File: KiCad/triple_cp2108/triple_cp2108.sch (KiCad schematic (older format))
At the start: 18 parts

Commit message: Parts importing in prgs.
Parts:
- gave numbers to parts that had none: 18
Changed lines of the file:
@@
 $EndDescr
 $Comp
-L Connector:USB_B J?
+L Connector:USB_B J1
 U 1 1 5FE5590A
 P 750 1000
-F 0 "J?" H 807 1467 50  0000 C CNN
+F 0 "J1" H 807 1467 50  0000 C CNN
 F 1 "USB_B" H 807 1376 50  0000 C CNN
 F 2 "" H 900 950 50  0001 C CNN
@@
 NoConn ~ 650  1400
 $Comp
-L power:GND #PWR?
+L power:GND #PWR0101
 U 1 1 5FE56D8C
 P 750 1700
-F 0 "#PWR?" H 750 1450 50  0001 C CNN
+F 0 "#PWR0101" H 750 1450 50  0001 C CNN
 F 1 "GND" H 755 1527 50  0000 C CNN
 F 2 "" H 750 1700 50  0001 C CNN
@@
 	1500 1100 1900 1100
 $Comp
-L Interface_USB:USB2514B_Bi U?
+L Interface_USB:USB2514B_Bi U2
 U 1 1 5FE587F7
 P 2700 5150
-F 0 "U?" H 3650 3700 50  0000 C CNN
+F 0 "U2" H 3650 3700 50  0000 C CNN
 F 1 "USB2514B_Bi" H 3450 3600 50  0000 C CNN
 F 2 "Package_DFN_QFN:QFN-36-1EP_6x6mm_P0.5mm_EP3.7x3.7mm" H 4000 3650 50  0001 C CNN
@@
 NoConn ~ 3800 6050
 $Comp
-L Regulator_Linear:MIC5504-3.3YM5 U?
+L Regulator_Linear:MIC5504-3.3YM5 U1
 U 1 1 5FE5BDFF
 P 1700 2400
-F 0 "U?" H 1700 2767 50  0000 C CNN
+F 0 "U1" H 1700 2767 50  0000 C CNN
 F 1 "MIC5504-3.3YM5" H 1700 2676 50  0000 C CNN
 F 2 "Package_TO_SOT_SMD:SOT-23-5" H 1700 2000 50  0001 C CNN
@@
 	1700 2700 1700 2800
 $Comp
-L power:GND #PWR?
+L power:GND #PWR0102
 U 1 1 5FE5FD67
 P 1700 2850
-F 0 "#PWR?" H 1700 2600 50  0001 C CNN
+F 0 "#PWR0102" H 1700 2600 50  0001 C CNN
 F 1 "GND" H 1705 2677 50  0000 C CNN
 F 2 "" H 1700 2850 50  0001 C CNN
@@
 $EndComp
 $Comp
-L Device:C C?
+L Device:C C3
 U 1 1 5FE61456
 P 1100 2550
-F 0 "C?" V 1150 2700 50  0000 C CNN
+F 0 "C3" V 1150 2700 50  0000 C CNN
 F 1 "1u" V 1150 2400 50  0000 C CNN
 F 2 "" H 1138 2400 50  0001 C CNN
@@
 	2150 2300 2250 2300
 $Comp
-L Device:C C?
+L Device:C C4
 U 1 1 5FE6AB30
 P 2150 2550
-F 0 "C?" V 2200 2700 50  0000 C CNN
+F 0 "C4" V 2200 2700 50  0000 C CNN
 F 1 "1u" V 2200 2400 50  0000 C CNN
 F 2 "" H 2188 2400 50  0001 C CNN
@@
 	2150 2300 2150 2400
 $Comp
-L Device:C C?
+L Device:C C5
 U 1 1 5FE79D1D
 P 2700 1200
-F 0 "C?" V 2750 1350 50  0000 C CNN
+F 0 "C5" V 2750 1350 50  0000 C CNN
 F 1 "4u7" V 2750 1050 50  0000 C CNN
 F 2 "" H 2738 1050 50  0001 C CNN
@@
 VBUS_5V
 $Comp
-L power:GND #PWR?
+L power:GND #PWR0103
 U 1 1 5FE7AB84
 P 2700 1450
-F 0 "#PWR?" H 2700 1200 50  0001 C CNN
+F 0 "#PWR0103" H 2700 1200 50  0001 C CNN
 F 1 "GND" H 2705 1277 50  0000 C CNN
 F 2 "" H 2700 1450 50  0001 C CNN
@@
 $EndComp
 $Comp
-L Device:C C?
+L Device:C C6
 U 1 1 5FE7B840
 P 2950 1200
-F 0 "C?" V 3000 1350 50  0000 C CNN
+F 0 "C6" V 3000 1350 50  0000 C CNN
 F 1 "4u7" V 3000 1050 50  0000 C CNN
 F 2 "" H 2988 1050 50  0001 C CNN
@@
 VBUS_5V
 $Comp
-L power:GND #PWR?
+L power:GND #PWR0104
 U 1 1 5FE7B849
 P 2950 1450
-F 0 "#PWR?" H 2950 1200 50  0001 C CNN
+F 0 "#PWR0104" H 2950 1200 50  0001 C CNN
 F 1 "GND" H 2955 1277 50  0000 C CNN
 F 2 "" H 2950 1450 50  0001 C CNN
@@
 $EndComp
 $Comp
-L Device:C C?
+L Device:C C7
 U 1 1 5FE7BF67
 P 3200 1200
-F 0 "C?" V 3250 1350 50  0000 C CNN
+F 0 "C7" V 3250 1350 50  0000 C CNN
 F 1 "4u7" V 3250 1050 50  0000 C CNN
 F 2 "" H 3238 1050 50  0001 C CNN
@@
 VBUS_5V
 $Comp
-L power:GND #PWR?
+L power:GND #PWR0105
 U 1 1 5FE7BF70
 P 3200 1450
-F 0 "#PWR?" H 3200 1200 50  0001 C CNN
+F 0 "#PWR0105" H 3200 1200 50  0001 C CNN
 F 1 "GND" H 3205 1277 50  0000 C CNN
 F 2 "" H 3200 1450 50  0001 C CNN
@@
 	2700 6650 2700 6700
 $Comp
-L power:GND #PWR?
+L power:GND #PWR0106
 U 1 1 5FE85EAB
 P 2700 6800
-F 0 "#PWR?" H 2700 6550 50  0001 C CNN
+F 0 "#PWR0106" H 2700 6550 50  0001 C CNN
 F 1 "GND" H 2705 6627 50  0000 C CNN
 F 2 "" H 2700 6800 50  0001 C CNN
@@
 D+_4
 $Comp
-L Device:Crystal_Small Y?
+L Device:Crystal_Small Y1
 U 1 1 5FE8EB29
 P 1200 5450
-F 0 "Y?" H 1300 5350 50  0000 C CNN
+F 0 "Y1" H 1300 5350 50  0000 C CNN
 F 1 "24M" H 1100 5350 50  0000 C CNN
 F 2 "" H 1200 5450 50  0001 C CNN
@@
 	1400 5650 1400 5600
 $Comp
-L Device:R R?
+L Device:R R1
 U 1 1 5FE92ED4
 P 1400 5450
-F 0 "R?" V 1300 5300 50  0000 L CNN
+F 0 "R1" V 1300 5300 50  0000 L CNN
 F 1 "1M" V 1300 5500 50  0000 L CNN
 F 2 "" V 1330 5450 50  0001 C CNN
@@
 Connection ~ 1400 5650
 $Comp
-L Device:C C?
+L Device:C C1
 U 1 1 5FE9A7F7
 P 900 5250
-F 0 "C?" V 800 5150 50  0000 C CNN
+F 0 "C1" V 800 5150 50  0000 C CNN
 F 1 "18p" V 800 5400 50  0000 C CNN
 F 2 "" H 938 5100 50  0001 C CNN
@@
 $EndComp
 $Comp
-L Device:C C?
+L Device:C C2
 U 1 1 5FE9B6E0
 P 900 5650
-F 0 "C?" V 1000 5550 50  0000 C CNN
+F 0 "C2" V 1000 5550 50  0000 C CNN
 F 1 "18p" V 1000 5800 50  0000 C CNN
 F 2 "" H 938 5500 50  0001 C CNN
@@
 	650  5650 650  5700
 $Comp
-L power:GND #PWR?
+L power:GND #PWR0107
 U 1 1 5FEA295F
 P 650 5300
-F 0 "#PWR?" H 650 5050 50  0001 C CNN
+F 0 "#PWR0107" H 650 5050 50  0001 C CNN
 F 1 "GND" H 655 5127 50  0000 C CNN
 F 2 "" H 650 5300 50  0001 C CNN
@@
 $EndComp
 $Comp
-L power:GND #PWR?
+L power:GND #PWR0108
 U 1 1 5FEA2CD9
 P 650 5700
-F 0 "#PWR?" H 650 5450 50  0001 C CNN
+F 0 "#PWR0108" H 650 5450 50  0001 C CNN
 F 1 "GND" H 655 5527 50  0000 C CNN
 F 2 "" H 650 5700 50  0001 C CNN
@@
 SUSP_IND
 $Comp
-L power:GND #PWR?
+L power:GND #PWR0109
 U 1 1 5FED890D
 P 4550 7000
-F 0 "#PWR?" H 4550 6750 50  0001 C CNN
+F 0 "#PWR0109" H 4550 6750 50  0001 C CNN
 F 1 "GND" H 4555 6827 50  0000 C CNN
 F 2 "" H 4550 7000 50  0001 C CNN
@@
 HS_IND
 $Comp
-L power:GND #PWR?
+L power:GND #PWR0110
 U 1 1 5FED891C
 P 4800 7000
-F 0 "#PWR?" H 4800 6750 50  0001 C CNN
+F 0 "#PWR0110" H 4800 6750 50  0001 C CNN
 F 1 "GND" H 4805 6827 50  0000 C CNN
 F 2 "" H 4800 7000 50  0001 C CNN
@@
 RBIAS
 $Comp
-L power:GND #PWR?
+L power:GND #PWR0111
 U 1 1 5FED892B
 P 5050 7000
-F 0 "#PWR?" H 5050 6750 50  0001 C CNN
+F 0 "#PWR0111" H 5050 6750 50  0001 C CNN
 F 1 "GND" H 5055 6827 50  0000 C CNN
 F 2 "" H 5050 7000 50  0001 C CNN
@@
 $EndComp
 $Comp
-L Device:R R?
+L Device:R R2
 U 1 1 5FEDAE4B
 P 4550 6750
-F 0 "R?" V 4450 6600 50  0000 L CNN
+F 0 "R2" V 4450 6600 50  0000 L CNN
 F 1 "56K" V 4450 6800 50  0000 L CNN
 F 2 "" V 4480 6750 50  0001 C CNN
@@
 $EndComp
 $Comp
-L Power_Protection:SP0503BAHT D?
+L Power_Protection:SP0503BAHT D1
 U 1 1 5FE57167
 P 1400 1400
-F 0 "D?" H 1605 1446 50  0000 L CNN
+F 0 "D1" H 1605 1446 50  0000 L CNN
 F 1 "SP0503BAHT" H 1605 1355 50  0000 L CNN
 F 2 "Package_TO_SOT_SMD:SOT-143" H 1625 1350 50  0001 L CNN
@@
 $EndComp
 $Comp
-L Device:R R?
+L Device:R R3
 U 1 1 5FEDC4C9
 P 4800 6750
-F 0 "R?" V 4700 6600 50  0000 L CNN
+F 0 "R3" V 4700 6600 50  0000 L CNN
 F 1 "56K" V 4700 6800 50  0000 L CNN
 F 2 "" V 4730 6750 50  0001 C CNN
@@
 $EndComp
 $Comp
-L Device:R R?
+L Device:R R4
 U 1 1 5FEDC7DE
 P 5050 6750
-F 0 "R?" V 4950 6600 50  0000 L CNN
+F 0 "R4" V 4950 6600 50  0000 L CNN
 F 1 "12k" V 4950 6800 50  0000 L CNN
 F 2 "" V 4980 6750 50  0001 C CNN
@@
 $EndComp
 $Comp
-L Connector:USB_A J?
+L Connector:USB_A J2
 U 1 1 5FEDCCF1
 P 4750 4850
-F 0 "J?" H 4807 5317 50  0000 C CNN
+F 0 "J2" H 4807 5317 50  0000 C CNN
 F 1 "USB_A" H 4807 5226 50  0000 C CNN
 F 2 "" H 4900 4800 50  0001 C CNN
@@
 NoConn ~ 4650 5250
 $Comp
-L power:GND #PWR?
+L power:GND #PWR0112
 U 1 1 5FEE0974
 P 4750 5550
-F 0 "#PWR?" H 4750 5300 50  0001 C CNN
+F 0 "#PWR0112" H 4750 5300 50  0001 C CNN
 F 1 "GND" H 4755 5377 50  0000 C CNN
 F 2 "" H 4750 5550 50  0001 C CNN
@@
 	5500 4950 5900 4950
 $Comp
-L Power_Protection:SP0503BAHT D?
+L Power_Protection:SP0503BAHT D2
 U 1 1 5FEE098B
 P 5400 5250
-F 0 "D?" H 5605 5296 50  0000 L CNN
+F 0 "D2" H 5605 5296 50  0000 L CNN
 F 1 "SP0503BAHT" H 5605 5205 50  0000 L CNN
 F 2 "Package_TO_SOT_SMD:SOT-143" H 5625 5200 50  0001 L CNN

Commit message: 2108 in prgs.
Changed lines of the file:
@@
 $Descr A4 11693 8268
 encoding utf-8
-Sheet 1 3
+Sheet 1 4
 Title ""
 Date ""
@@
 $EndComp
 $Sheet
-S 8100 2450 550  750
+S 8300 1450 550  750
 U 5FEF445C
 F0 "2108_Block A" 50
@@
 $EndSheet
 $Sheet
-S 8100 3850 550  750
+S 8300 2850 550  750
 U 5FEFA5BE
 F0 "2108_Block B" 50
 F1 "2108.sch" 50
 $EndSheet
+$Sheet
+S 8300 4250 550  750
+U 6001CD0C
+F0 "2108_Block C" 50
+F1 "2108.sch" 50
+$EndSheet

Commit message: GPIO Consolidation in prgs.
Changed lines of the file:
@@
 $EndComp
 $Sheet
-S 8300 1450 550  750
+S 7300 600  800  900
+U 5FEFA5BE
+F0 "2108_Block B" 50
+F1 "2108.sch" 50
+F2 "VBUS_5V" I L 7300 700 50
+F3 "D-" I L 7300 800 50
+F4 "D+" I L 7300 900 50
+F5 "GND" I L 7300 1000 50
+F6 "GPIO2" I R 8100 700 50
+F7 "GPIO3" I R 8100 800 50
+F8 "GPIO6" I R 8100 900 50
+F9 "GPIO7" I R 8100 1000 50
+F10 "GPIO10" I R 8100 1100 50
+F11 "GPIO11" I R 8100 1200 50
+F12 "GPIO14" I R 8100 1300 50
+F13 "GPIO15" I R 8100 1400 50
+$EndSheet
+$Sheet
+S 9450 600  800  900
+U 6001CD0C
+F0 "2108_Block C" 50
+F1 "2108.sch" 50
+F2 "VBUS_5V" I L 9450 700 50
+F3 "D-" I L 9450 800 50
+F4 "D+" I L 9450 900 50
+F5 "GND" I L 9450 1000 50
+F6 "GPIO2" I R 10250 700 50
+F7 "GPIO3" I R 10250 800 50
+F8 "GPIO6" I R 10250 900 50
+F9 "GPIO7" I R 10250 1000 50
+F10 "GPIO10" I R 10250 1100 50
+F11 "GPIO11" I R 10250 1200 50
+F12 "GPIO14" I R 10250 1300 50
+F13 "GPIO15" I R 10250 1400 50
+$EndSheet
+Text Label 4600 700  2    50   ~ 0
+VBUS_5V
+Wire Wire Line
+	4600 700  4750 700
+Text Label 4600 800  2    50   ~ 0
+D-_1
+Wire Wire Line
+	4600 800  4750 800
+Text Label 4600 900  2    50   ~ 0
+D+_1
+Wire Wire Line
+	4600 900  4750 900
+Wire Wire Line
+	4750 1000 4650 1000
+Wire Wire Line
+	4650 1000 4650 1050
+$Comp
+L power:GND #PWR?
+U 1 1 60B7F1E8
+P 4650 1050
+F 0 "#PWR?" H 4650 800 50  0001 C CNN
+F 1 "GND" H 4655 877 50  0000 C CNN
+F 2 "" H 4650 1050 50  0001 C CNN
+F 3 "" H 4650 1050 50  0001 C CNN
+	1    4650 1050
+	1    0    0    -1
+$EndComp
+Text Label 7150 700  2    50   ~ 0
+VBUS_5V
+Wire Wire Line
+	7150 700  7300 700
+Text Label 7150 800  2    50   ~ 0
+D-_2
+Wire Wire Line
+	7150 800  7300 800
+Text Label 7150 900  2    50   ~ 0
+D+_2
+Wire Wire Line
+	7150 900  7300 900
+Wire Wire Line
+	7300 1000 7200 1000
+Wire Wire Line
+	7200 1000 7200 1050
+$Comp
+L power:GND #PWR?
+U 1 1 60B7FF16
+P 7200 1050
+F 0 "#PWR?" H 7200 800 50  0001 C CNN
+F 1 "GND" H 7205 877 50  0000 C CNN
+F 2 "" H 7200 1050 50  0001 C CNN
+F 3 "" H 7200 1050 50  0001 C CNN
+	1    7200 1050
+	1    0    0    -1
+$EndComp
+Text Label 9300 700  2    50   ~ 0
+VBUS_5V
+Wire Wire Line
+	9300 700  9450 700
+Text Label 9300 800  2    50   ~ 0
+D-_3
+Wire Wire Line
+	9300 800  9450 800
+Text Label 9300 900  2    50   ~ 0
+D+_3
+Wire Wire Line
+	9300 900  9450 900
+Wire Wire Line
+	9450 1000 9350 1000
+Wire Wire Line
+	9350 1000 9350 1050
+$Comp
+L power:GND #PWR?
+U 1 1 60B83431
+P 9350 1050
+F 0 "#PWR?" H 9350 800 50  0001 C CNN
+F 1 "GND" H 9355 877 50  0000 C CNN
+F 2 "" H 9350 1050 50  0001 C CNN
+F 3 "" H 9350 1050 50  0001 C CNN
+	1    9350 1050
+	1    0    0    -1
+$EndComp
+$Sheet
+S 4750 600  800  900
 U 5FEF445C
 F0 "2108_Block A" 50
 F1 "2108.sch" 50
-$EndSheet
-$Sheet
-S 8300 2850 550  750
-U 5FEFA5BE
-F0 "2108_Block B" 50
-F1 "2108.sch" 50
-$EndSheet
-$Sheet
-S 8300 4250 550  750
-U 6001CD0C
-F0 "2108_Block C" 50
-F1 "2108.sch" 50
+F2 "VBUS_5V" I L 4750 700 50
+F3 "D-" I L 4750 800 50
+F4 "D+" I L 4750 900 50
+F5 "GND" I L 4750 1000 50
+F6 "GPIO2" I R 5550 700 50
+F7 "GPIO3" I R 5550 800 50
+F8 "GPIO6" I R 5550 900 50
+F9 "GPIO7" I R 5550 1000 50
+F10 "GPIO10" I R 5550 1100 50
+F11 "GPIO11" I R 5550 1200 50
+F12 "GPIO14" I R 5550 1300 50
+F13 "GPIO15" I R 5550 1400 50
 $EndSheet
 $EndSCHEMATC

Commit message: misc.
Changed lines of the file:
@@
 F4 "D+" I L 7300 900 50
 F5 "GND" I L 7300 1000 50
-F6 "GPIO2" I R 8100 700 50
-F7 "GPIO3" I R 8100 800 50
-F8 "GPIO6" I R 8100 900 50
-F9 "GPIO7" I R 8100 1000 50
-F10 "GPIO10" I R 8100 1100 50
-F11 "GPIO11" I R 8100 1200 50
-F12 "GPIO14" I R 8100 1300 50
-F13 "GPIO15" I R 8100 1400 50
+F6 "GPIO2" B R 8100 700 50
+F7 "GPIO3" B R 8100 800 50
+F8 "GPIO6" B R 8100 900 50
+F9 "GPIO7" B R 8100 1000 50
+F10 "GPIO10" B R 8100 1100 50
+F11 "GPIO11" B R 8100 1200 50
+F12 "GPIO14" B R 8100 1300 50
+F13 "GPIO15" B R 8100 1400 50
 $EndSheet
 $Sheet
@@
 F4 "D+" I L 9450 900 50
 F5 "GND" I L 9450 1000 50
-F6 "GPIO2" I R 10250 700 50
-F7 "GPIO3" I R 10250 800 50
-F8 "GPIO6" I R 10250 900 50
-F9 "GPIO7" I R 10250 1000 50
-F10 "GPIO10" I R 10250 1100 50
-F11 "GPIO11" I R 10250 1200 50
-F12 "GPIO14" I R 10250 1300 50
-F13 "GPIO15" I R 10250 1400 50
+F6 "GPIO2" B R 10250 700 50
+F7 "GPIO3" B R 10250 800 50
+F8 "GPIO6" B R 10250 900 50
+F9 "GPIO7" B R 10250 1000 50
+F10 "GPIO10" B R 10250 1100 50
+F11 "GPIO11" B R 10250 1200 50
+F12 "GPIO14" B R 10250 1300 50
+F13 "GPIO15" B R 10250 1400 50
 $EndSheet
 Text Label 4600 700  2    50   ~ 0
@@
 	4650 1000 4650 1050
 $Comp
-L power:GND #PWR?
+L power:GND #PWR0113
 U 1 1 60B7F1E8
 P 4650 1050
-F 0 "#PWR?" H 4650 800 50  0001 C CNN
+F 0 "#PWR0113" H 4650 800 50  0001 C CNN
 F 1 "GND" H 4655 877 50  0000 C CNN
 F 2 "" H 4650 1050 50  0001 C CNN
@@
 	7200 1000 7200 1050
 $Comp
-L power:GND #PWR?
+L power:GND #PWR0114
 U 1 1 60B7FF16
 P 7200 1050
-F 0 "#PWR?" H 7200 800 50  0001 C CNN
+F 0 "#PWR0114" H 7200 800 50  0001 C CNN
 F 1 "GND" H 7205 877 50  0000 C CNN
 F 2 "" H 7200 1050 50  0001 C CNN
@@
 	9350 1000 9350 1050
 $Comp
-L power:GND #PWR?
+L power:GND #PWR0115
 U 1 1 60B83431
 P 9350 1050
-F 0 "#PWR?" H 9350 800 50  0001 C CNN
+F 0 "#PWR0115" H 9350 800 50  0001 C CNN
 F 1 "GND" H 9355 877 50  0000 C CNN
 F 2 "" H 9350 1050 50  0001 C CNN
@@
 F4 "D+" I L 4750 900 50
 F5 "GND" I L 4750 1000 50
-F6 "GPIO2" I R 5550 700 50
-F7 "GPIO3" I R 5550 800 50
-F8 "GPIO6" I R 5550 900 50
-F9 "GPIO7" I R 5550 1000 50
-F10 "GPIO10" I R 5550 1100 50
-F11 "GPIO11" I R 5550 1200 50
-F12 "GPIO14" I R 5550 1300 50
-F13 "GPIO15" I R 5550 1400 50
+F6 "GPIO3" B R 5550 800 50
+F7 "GPIO2" B R 5550 700 50
+F8 "GPIO6" B R 5550 900 50
+F9 "GPIO7" B R 5550 1000 50
+F10 "GPIO10" B R 5550 1100 50
+F11 "GPIO11" B R 5550 1200 50
+F12 "GPIO14" B R 5550 1300 50
+F13 "GPIO15" B R 5550 1400 50
 $EndSheet
 $EndSCHEMATC

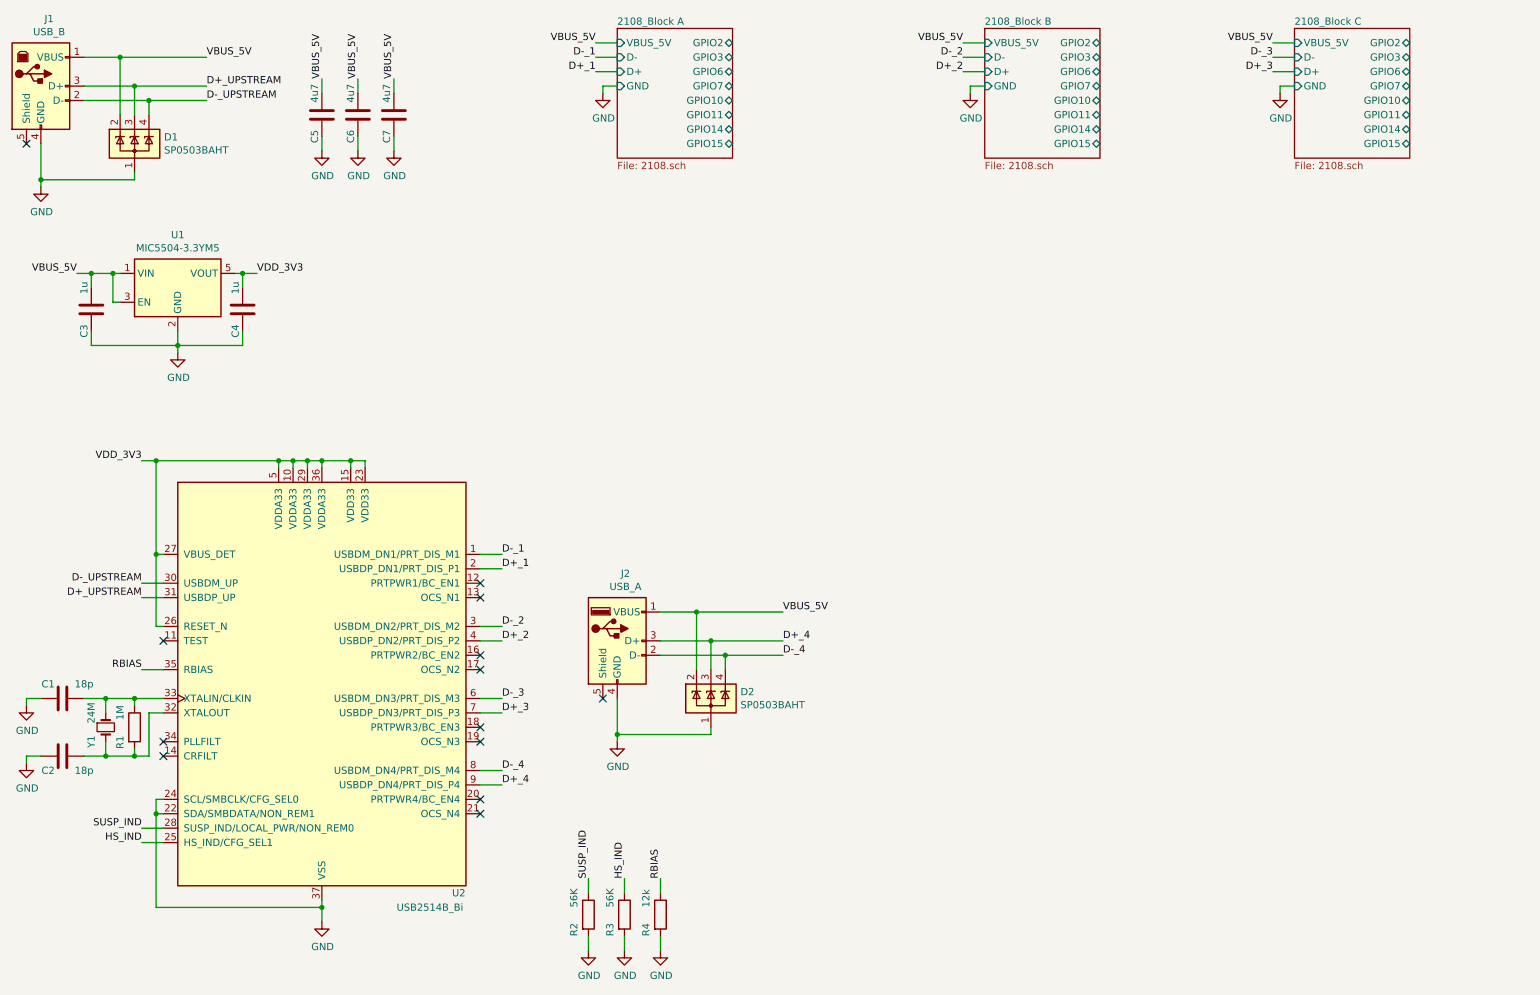
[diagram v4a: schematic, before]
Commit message: Diodes changed
USB ESD protection diodes changed to individual ones
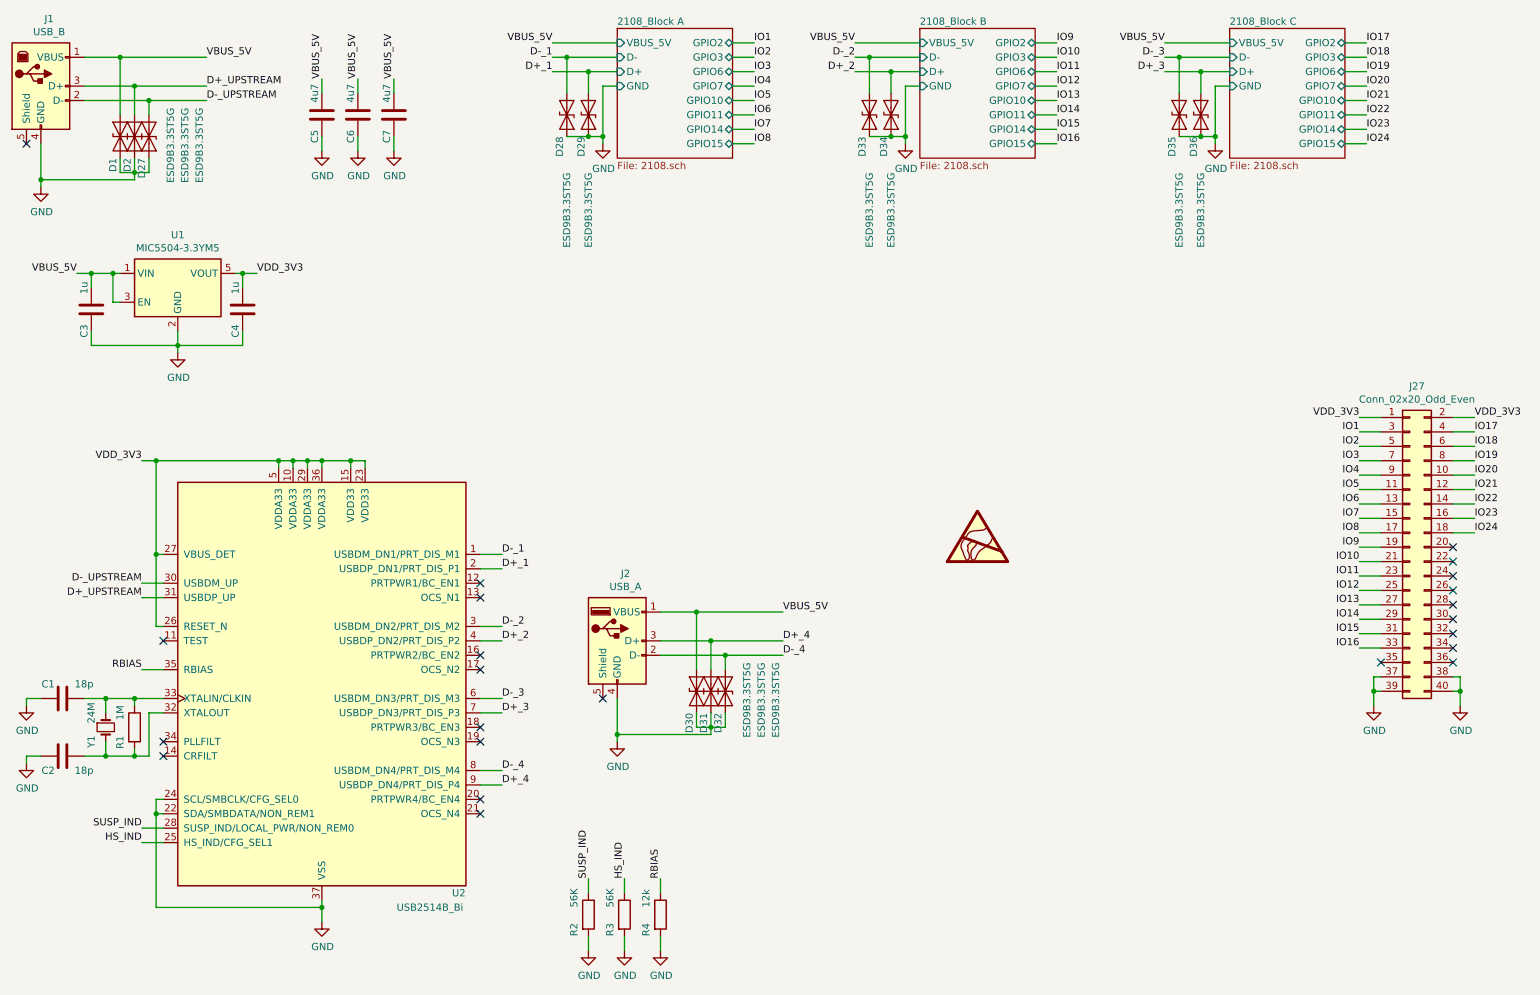
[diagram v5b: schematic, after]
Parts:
- removed D1, D2: SP0503BAHT, Package_TO_SOT_SMD:SOT-143, symbol Power_Protection:SP0503BAHT
- added D1, D2, D27, D28, D29, D30, D31, D32, D33, D34, D35, D36: ESD9B3.3ST5G, Diode_SMD:D_SOD-923, symbol Diode:ESD9B3.3ST5G
- added J27: Conn_02x20_Odd_Even, symbol Connector_Generic:Conn_02x20_Odd_Even
- C1, C2, C3, C4, C5, C6, C7: footprint (none) -> Capacitor_SMD:C_2225_5664Metric
- J1: footprint (none) -> Connector_USB:USB_B_OST_USB-B1HSxx_Horizontal
- J2: footprint (none) -> Connector_USB:USB_A_CONNFLY_DS1095-WNR0
- R1, R2, R3, R4: footprint (none) -> Resistor_SMD:R_1206_3216Metric
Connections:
- net D+_1: now also D29.1 (A1)
- net D+_2: now also D34.1 (A1)
- net D+_3: now also D36.1 (A1)
- net D+_4: now also D31.1 (A1)
- net D+_UPSTREAM: now also D2.1 (A1)
- net D-_1: now also D28.1 (A1)
- net D-_2: now also D33.1 (A1)
- net D-_3: now also D35.1 (A1)
- net D-_4: now also D32.1 (A1)
- net D-_UPSTREAM: now also D27.1 (A1)
- net GND: now also D1.2 (A2), D2.2 (A2), D27.2 (A2), D28.2 (A2), D29.2 (A2), D30.2 (A2), D31.2 (A2), D32.2 (A2), D33.2 (A2), D34.2 (A2), D35.2 (A2), D36.2 (A2), J27.37 (Pin_37), J27.38 (Pin_38), J27.39 (Pin_39), J27.40 (Pin_40)
- net VBUS_5V: now also D1.1 (A1), D30.1 (A1)
- net VDD_3V3: now also J27.1 (Pin_1), J27.2 (Pin_2)
- new net IO1: J27.3 (Pin_3)
- new net IO10: J27.21 (Pin_21)
- new net IO11: J27.23 (Pin_23)
- new net IO12: J27.25 (Pin_25)
- new net IO13: J27.27 (Pin_27)
- new net IO14: J27.29 (Pin_29)
- new net IO15: J27.31 (Pin_31)
- new net IO16: J27.33 (Pin_33)
- new net IO17: J27.4 (Pin_4)
- new net IO18: J27.6 (Pin_6)
- new net IO19: J27.8 (Pin_8)
- new net IO2: J27.5 (Pin_5)
- new net IO20: J27.10 (Pin_10)
- new net IO21: J27.12 (Pin_12)
- new net IO22: J27.14 (Pin_14)
- new net IO23: J27.16 (Pin_16)
- new net IO24: J27.18 (Pin_18)
- new net IO3: J27.7 (Pin_7)
- new net IO4: J27.9 (Pin_9)
- new net IO5: J27.11 (Pin_11)
- new net IO6: J27.13 (Pin_13)
- new net IO7: J27.15 (Pin_15)
- new net IO8: J27.17 (Pin_17)
- new net IO9: J27.19 (Pin_19)
- no-connect marks 13 -> 23
